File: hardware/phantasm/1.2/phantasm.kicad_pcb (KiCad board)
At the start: 4 copper layers, 58.3 x 32 mm, 33 parts, among them J1 TBC05-02-1-G-G +5V IN ~1A, J2 TBC05-03-1-G-G LED DI/SIG_GND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, J3A TBC05-03-1-G-G SYNC in, J3B TBC05-03-1-G-G SYNC out, J4 debug, U1 74AHCT125

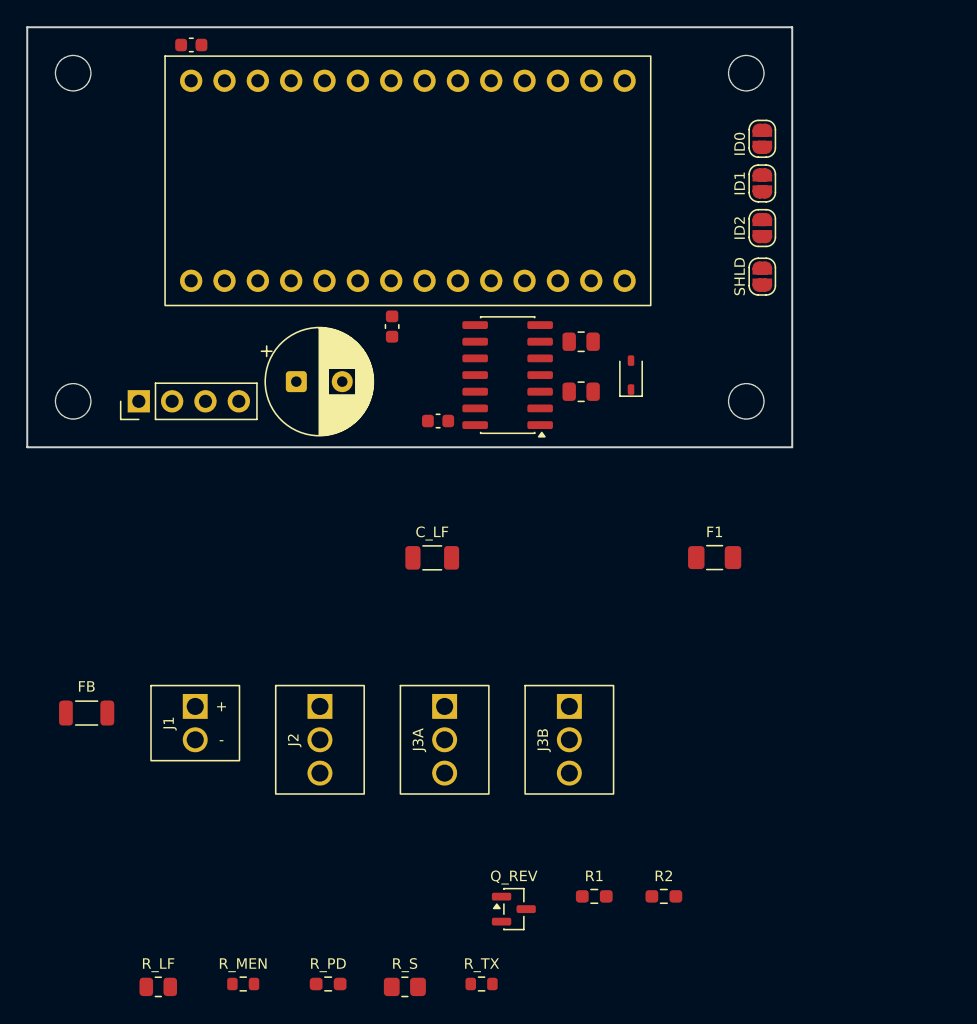
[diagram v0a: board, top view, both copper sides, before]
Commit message: pcb: enforce edge connector placement and wire clearance
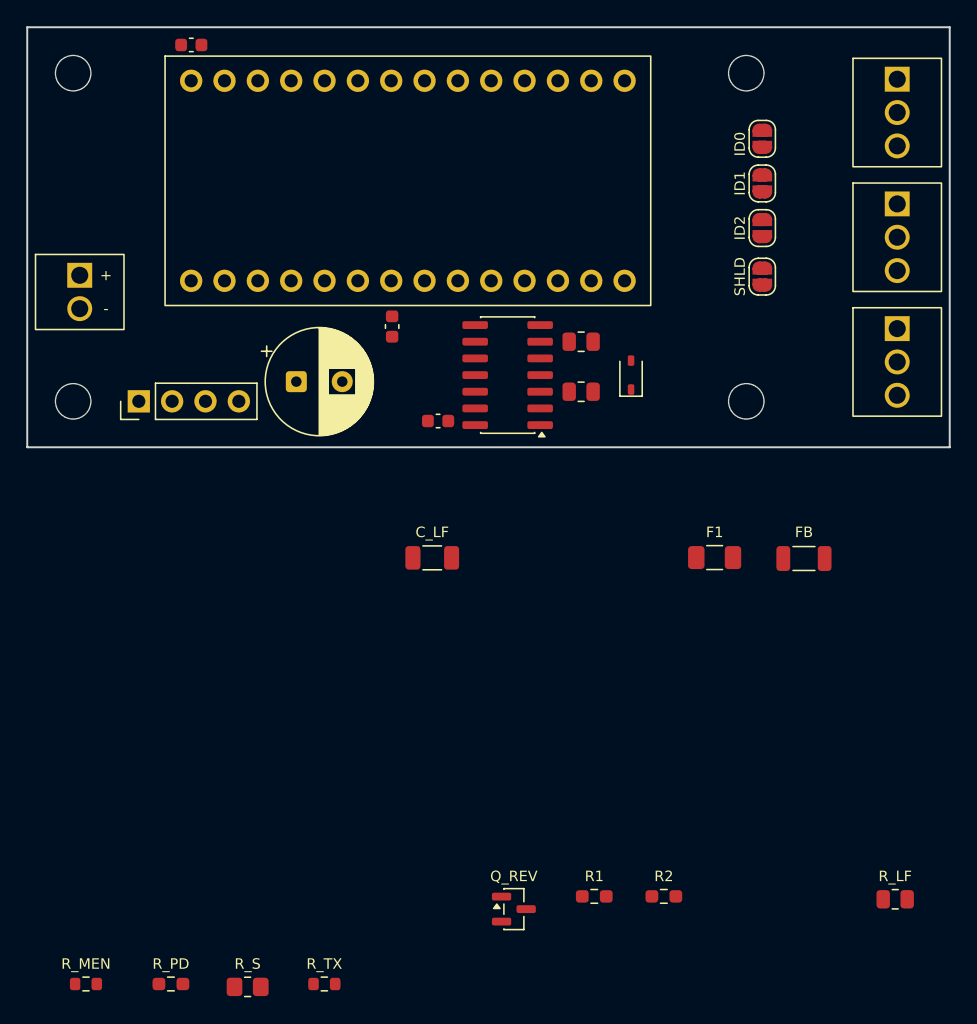
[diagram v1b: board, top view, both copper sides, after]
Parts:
- moved J2 64.9 mm to (66.3, 3.96)
- moved R_LF 56.5 mm to (66.1, 66.4)
- moved FB 55.9 mm to (59.2, 40.5)
- moved J3A 51.5 mm to (66.3, 13.5)
- moved J3B 38.1 mm to (66.3, 23.0)
- moved J1 34.0 mm to (4.00, 18.9)
- moved R_PD 12.0 mm to (10.9, 72.9)
- moved R_S 12.0 mm to (16.8, 73.1)
- moved R_TX 12.0 mm to (22.6, 72.9)
- moved R_MEN 12.0 mm to (4.47, 72.9)
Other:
- board size 58.3 x 32 mm -> 70.3 x 32 mm
- board text added: "LED OUT"
- board text added: "PHANTASM segment board UNPLACED - 70.28x32mm outline (width <=35mm); mechanical and signal-integrity placements locked"
- board text added: "PWR"
- board text added: "SYNC IN"
- board text added: "SYNC OUT"
- board text removed: "PHANTASM segment board UNPLACED - 58.28x32mm outline (width <=35mm); mechanical and signal-integrity placements locked"

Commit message: pcb: fit protected terminal bodies within the original outline
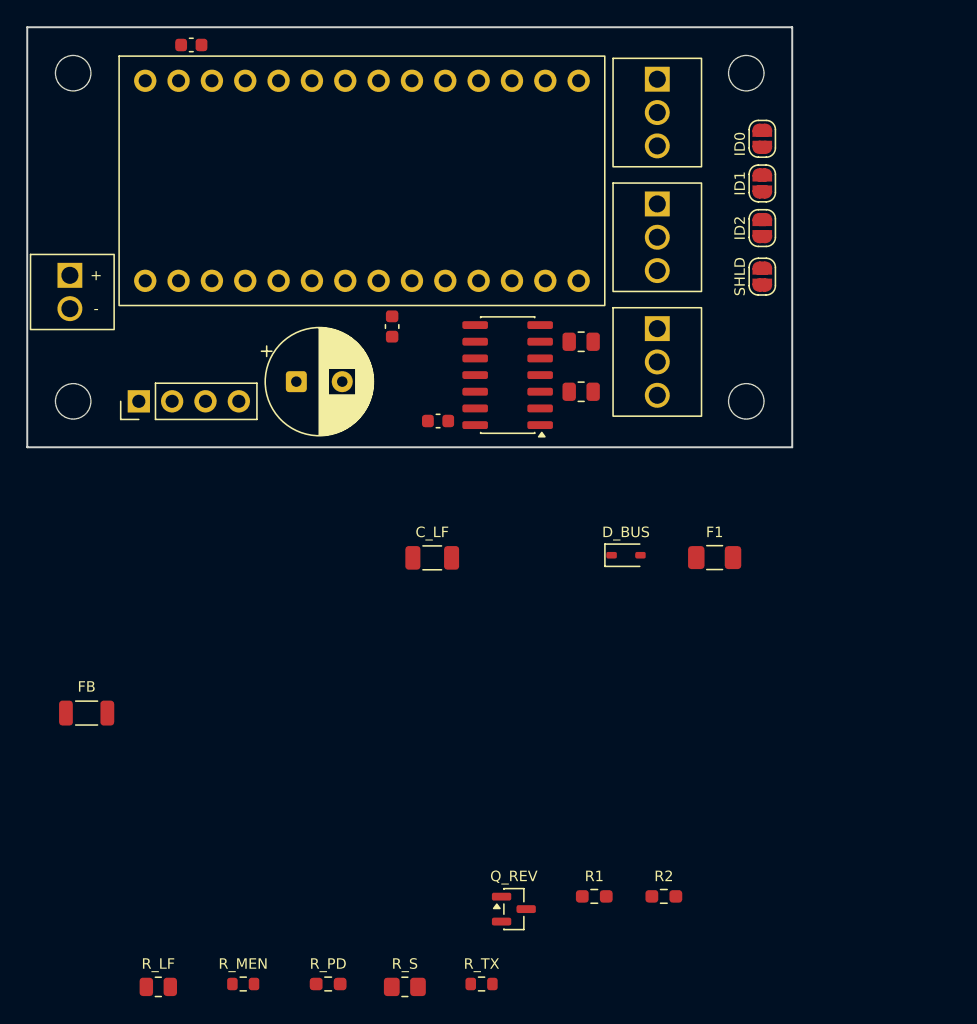
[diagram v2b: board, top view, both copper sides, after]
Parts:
- moved R_LF 56.5 mm to (9.98, 73.1)
- moved FB 55.9 mm to (4.53, 52.2)
- moved J2 18.3 mm to (48.0, 3.96)
- moved J3A 18.3 mm to (48.0, 13.5)
- moved J3B 18.3 mm to (48.0, 23.0)
- moved D_BUS 13.7 mm to (45.6, 40.2), turned to 0 degrees
- moved R_PD 12.0 mm to (22.9, 72.9)
- moved R_S 12.0 mm to (28.8, 73.1)
- moved R_TX 12.0 mm to (34.6, 72.9)
- moved R_MEN 12.0 mm to (16.5, 72.9)
- moved U_MCU 3.50 mm to (25.5, 11.7)
- moved J1 0.75 mm to (3.25, 18.9)
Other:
- board size 70.3 x 32 mm -> 58.3 x 32 mm
- board text added: "PHANTASM segment board UNPLACED - 58.28x32mm outline (width <=35mm); mechanical and signal-integrity placements locked"
- board text removed: "PHANTASM segment board UNPLACED - 70.28x32mm outline (width <=35mm); mechanical and signal-integrity placements locked"

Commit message: pcb: remove unused rev 1.2 debug header and serial connection
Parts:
- removed the H4 at (54.8, 28.5)
- H1: renamed from J4; value debug -> M2.5; footprint Connector_PinHeader_2.54mm:PinHeader_1x04_P2.54mm_Vertical -> MountingHole:MountingHole_2.7mm_M2.5
- moved H3 57.0 mm to (54.8, 3.50)
- moved H1 25.5 mm to (3.50, 3.50), turned to 0 degrees
- moved H2 25.0 mm to (3.50, 28.5)
- moved H4 25.0 mm to (54.8, 28.5)
- moved R1 3.42 mm to (43.2, 62.8)
- moved R2 3.42 mm to (48.5, 62.8)
- moved R_LF 3.42 mm to (9.98, 69.7)
- moved R_MEN 3.42 mm to (16.5, 69.5)
- moved R_PD 3.42 mm to (22.9, 69.5)
- moved R_S 3.42 mm to (28.8, 69.7)
- moved R_TX 3.42 mm to (34.6, 69.5)
- moved Q_REV 3.41 mm to (37.1, 63.8)
- renumbered H1 to H2, H2 to H3, H3 to H4
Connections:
- U_MCU pad 1: /SERIAL1_TX -> unconnected-(U_MCU-D1/TX1-Pad1)

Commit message: pcb: clarify bypass parents and enforce upload via minimum
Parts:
- C_DEC2: renamed from R_TX; value 10k -> 0.1uF; footprint Resistor_SMD:R_0603_1608Metric -> Capacitor_SMD:C_0603_1608Metric
- R_D1: renamed from U1; value 74AHCT125 -> 33R; footprint Package_SO:SOIC-14_3.9x8.7mm_P1.27mm -> Resistor_SMD:R_0805_2012Metric
- R_S: renamed from R_D2; value 33R -> 100R; footprint Resistor_SMD:R_0805_2012Metric -> Resistor_SMD:R_0805_2012Metric_Pad1.20x1.40mm_HandSolder
- R_TX: renamed from R_S; value 100R -> 10k; footprint Resistor_SMD:R_0805_2012Metric_Pad1.20x1.40mm_HandSolder -> Resistor_SMD:R_0603_1608Metric
- U1: renamed from U_MCU; value Teensy4.0 -> 74AHCT125; footprint phantasm:Teensy4.0 -> Package_SO:SOIC-14_3.9x8.7mm_P1.27mm
- U_MCU: renamed from C_DEC1; value 0.1uF -> Teensy4.0; footprint Capacitor_SMD:C_0603_1608Metric -> phantasm:Teensy4.0
- moved R_S 47.7 mm to (28.8, 69.7), turned to 0 degrees
- moved C_DEC2 39.6 mm to (31.3, 30.0), turned to 180 degrees
- moved C_DEC1 34.3 mm to (12.5, 1.35), turned to 0 degrees
- moved U1 18.5 mm to (36.6, 26.5), turned to 180 degrees
- moved U_MCU 16.6 mm to (25.5, 11.7)
- moved R_TX 5.85 mm to (34.6, 69.5)
- moved R_D1 5.74 mm to (42.2, 27.8)
- moved R_D2 3.81 mm to (42.2, 24.0)
- renumbered C_DEC2 to C_DEC1, R_D1 to R_D2
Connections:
- C_DEC2 pad 1: /SYNC_TX -> +5V_LOGIC
- R_D1 pad 1: GND -> /DATA
- R_D1 pad 2: /DATA_IN -> /DATA_SRC
- R_D2 pad 1: /DATA -> /CLK
- R_D2 pad 2: /DATA_SRC -> /CLK_SRC
- R_S pad 1: /CLK -> /SYNC_BUS
- R_S pad 2: /CLK_SRC -> /SYNC_SRC
- R_TX pad 1: /SYNC_BUS -> /SYNC_TX
- R_TX pad 2: /SYNC_SRC -> GND
- U1 pad 1: unconnected-(U_MCU-D1/TX1-Pad1) -> GND
- U1 pad 10: unconnected-(U_MCU-D10-Pad10) -> /MASTER_EN
- U1 pad 11: /DATA_IN -> /SYNC_PULLDOWN
- U1 pad 12: unconnected-(U_MCU-D12-Pad12) -> GND
- U1 pad 13: /CLK_IN -> /MASTER_EN
- U1 pad 14: unconnected-(U_MCU-D14-Pad14) -> +5V_LOGIC
- U1 pad 2: unconnected-(U_MCU-D2-Pad2) -> /DATA_IN
- U1 pad 3: /FRAME_SYNC -> /DATA_SRC
- U1 pad 4: /SYNC_TX -> GND
- U1 pad 5: /MASTER_EN -> /CLK_IN
- U1 pad 6: unconnected-(U_MCU-D6-Pad6) -> /CLK_SRC
- U1 pad 7: unconnected-(U_MCU-D7-Pad7) -> GND
- U1 pad 8: unconnected-(U_MCU-D8-Pad8) -> /SYNC_SRC
- U1 pad 9: unconnected-(U_MCU-D9-Pad9) -> /SYNC_TX
- U_MCU pad 1: +5V_LOGIC -> unconnected-(U_MCU-D1/TX1-Pad1)
- U_MCU pad 2: GND -> unconnected-(U_MCU-D2-Pad2)

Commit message: pcb: keep locked decouplers within 3 mm of supply pins
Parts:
- moved C_DEC1 2.75 mm to (9.75, 1.35)
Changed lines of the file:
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@@
 	(footprint "Capacitor_SMD:C_0603_1608Metric"
 		(locked yes)
-		(at 12.5 1.35 0)
+		(at 9.75 1.35 0)
 		(layer "F.Cu")
 		(descr "Capacitor SMD 0603 (1608 Metric), square (rectangular) end terminal, IPC-7351 nominal, (Body size source: IPC-SM-782 page 76, https://www.pcb-3d.com/wordpress/wp-content/uploads/ipc-sm-782a_amendment_1_and_2.pdf)")

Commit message: pcb: label every signal terminal pin (finding 81)
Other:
- board text added: "C"
- board text added: "D"
- board text added: "G"
- board text added: "H"
- board text added: "S"
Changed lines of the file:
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@@
 		(embedded_fonts no)
 	)
+	(gr_text "D" (at 52.5 3.96 0) (layer "F.SilkS") (effects (font (size 0.8 0.8) (thickness 0.15))))
+	(gr_text "G" (at 52.5 6.50 0) (layer "F.SilkS") (effects (font (size 0.8 0.8) (thickness 0.15))))
+	(gr_text "C" (at 52.5 9.04 0) (layer "F.SilkS") (effects (font (size 0.8 0.8) (thickness 0.15))))
+	(gr_text "S" (at 52.5 13.46 0) (layer "F.SilkS") (effects (font (size 0.8 0.8) (thickness 0.15))))
+	(gr_text "G" (at 52.5 16.00 0) (layer "F.SilkS") (effects (font (size 0.8 0.8) (thickness 0.15))))
+	(gr_text "H" (at 52.5 18.54 0) (layer "F.SilkS") (effects (font (size 0.8 0.8) (thickness 0.15))))
+	(gr_text "S" (at 52.5 22.96 0) (layer "F.SilkS") (effects (font (size 0.8 0.8) (thickness 0.15))))
+	(gr_text "G" (at 52.5 25.50 0) (layer "F.SilkS") (effects (font (size 0.8 0.8) (thickness 0.15))))
+	(gr_text "H" (at 52.5 28.04 0) (layer "F.SilkS") (effects (font (size 0.8 0.8) (thickness 0.15))))
 )

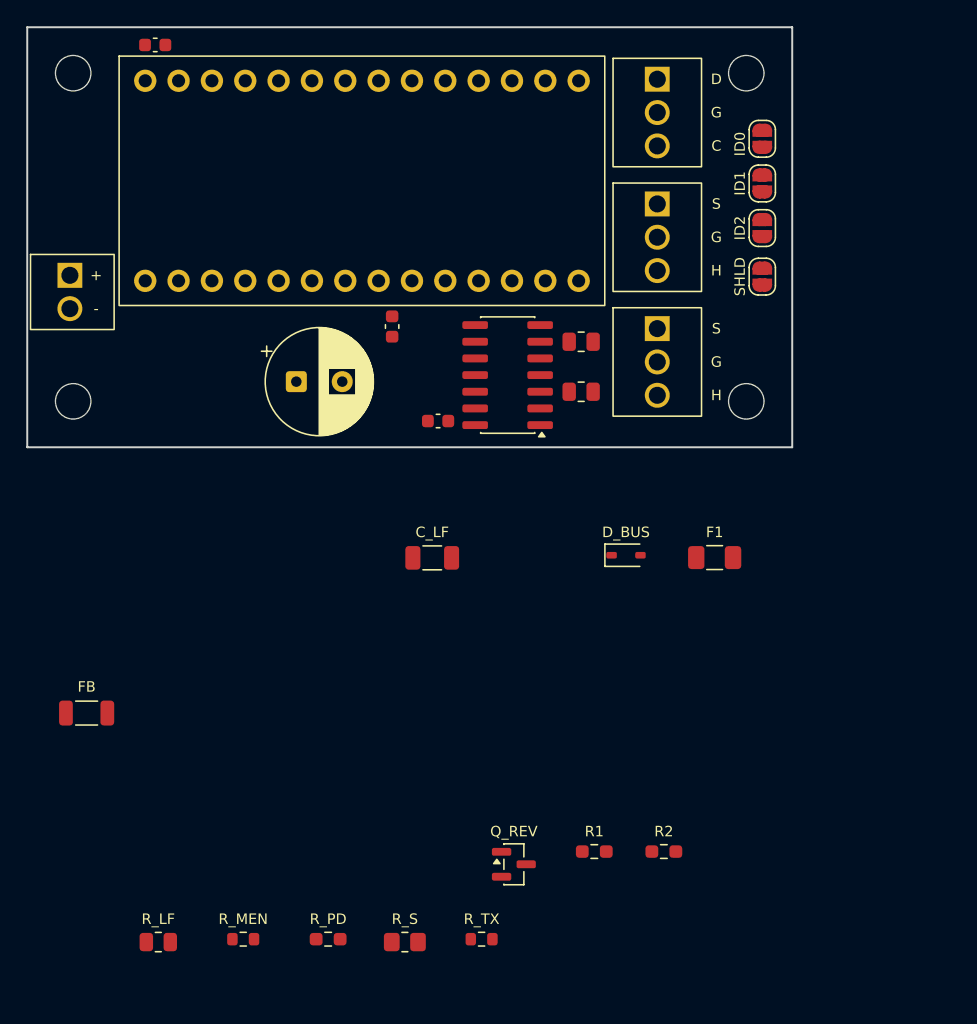
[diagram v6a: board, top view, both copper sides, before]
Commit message: pcb: pre-route the sync receive filter beside D3 (finding 4)
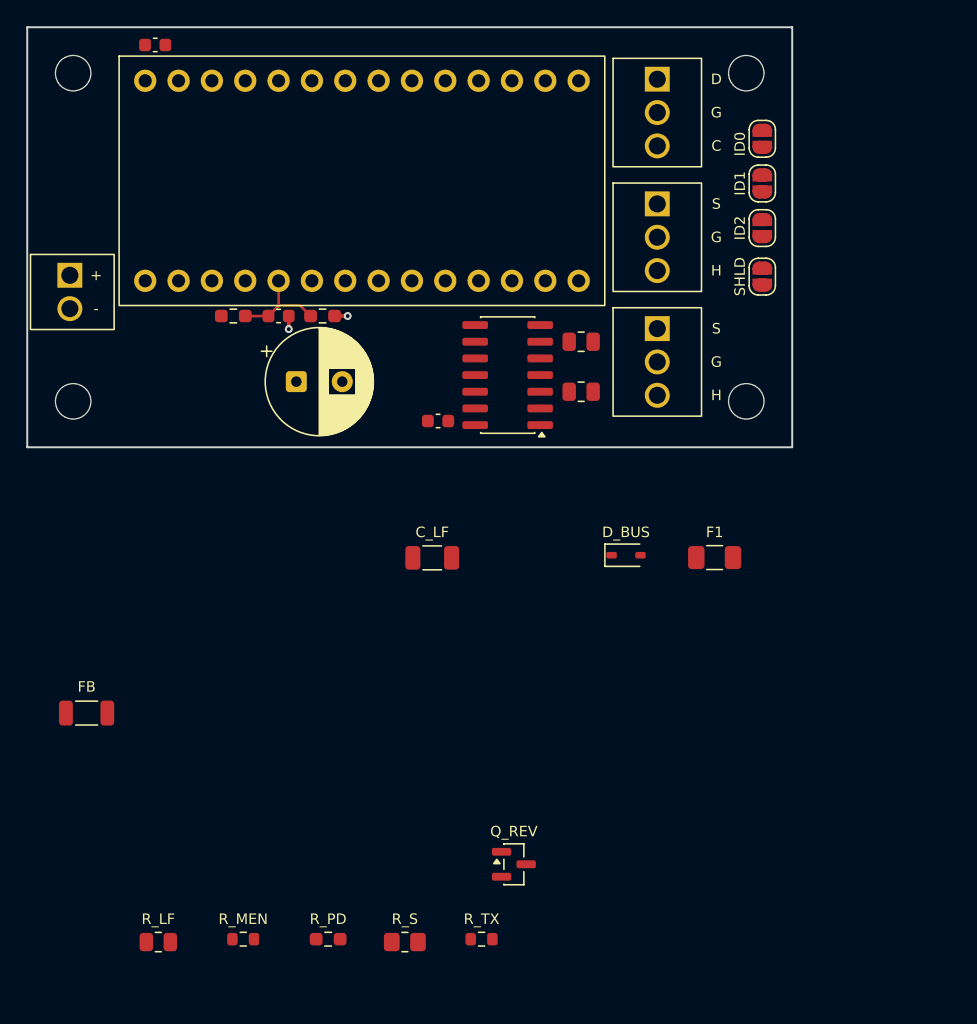
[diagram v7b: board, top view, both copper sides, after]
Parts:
- moved R1 49.2 mm to (15.7, 22.0)
- moved R2 48.4 mm to (22.5, 22.0)
- moved C_SYNC 8.69 mm to (19.1, 22.0), turned to 0 degrees
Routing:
- net /FRAME_SYNC: track 0.00 -> 8.64 mm
- net GND: track 0.00 -> 2.00 mm, vias 0 -> 2
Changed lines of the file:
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@@
 	(gr_text "ID2" (at 54.3 15.3 90) (layer "F.SilkS") (effects (font (size 0.8 0.8) (thickness 0.15))))
 	(gr_text "SHLD" (at 54.3 19 90) (layer "F.SilkS") (effects (font (size 0.8 0.8) (thickness 0.15))))
+	(gr_text "D" (at 52.5 3.96 0) (layer "F.SilkS") (effects (font (size 0.8 0.8) (thickness 0.15))))
+	(gr_text "G" (at 52.5 6.5 0) (layer "F.SilkS") (effects (font (size 0.8 0.8) (thickness 0.15))))
+	(gr_text "C" (at 52.5 9.04 0) (layer "F.SilkS") (effects (font (size 0.8 0.8) (thickness 0.15))))
+	(gr_text "S" (at 52.5 13.46 0) (layer "F.SilkS") (effects (font (size 0.8 0.8) (thickness 0.15))))
+	(gr_text "G" (at 52.5 16 0) (layer "F.SilkS") (effects (font (size 0.8 0.8) (thickness 0.15))))
+	(gr_text "H" (at 52.5 18.54 0) (layer "F.SilkS") (effects (font (size 0.8 0.8) (thickness 0.15))))
+	(gr_text "S" (at 52.5 22.96 0) (layer "F.SilkS") (effects (font (size 0.8 0.8) (thickness 0.15))))
+	(gr_text "G" (at 52.5 25.5 0) (layer "F.SilkS") (effects (font (size 0.8 0.8) (thickness 0.15))))
+	(gr_text "H" (at 52.5 28.04 0) (layer "F.SilkS") (effects (font (size 0.8 0.8) (thickness 0.15))))
 	(gr_text "PWR" (at 5.25 20.17 90) (layer "B.SilkS") (effects (font (size 0.8 0.8) (thickness 0.15)) (justify mirror)))
 	(gr_text "LED OUT" (at 46 6.5 90) (layer "B.SilkS") (effects (font (size 0.8 0.8) (thickness 0.15)) (justify mirror)))
@@
 	)
 	(footprint "Resistor_SMD:R_0603_1608Metric_Pad0.98x0.95mm_HandSolder"
+		(locked yes)
+		(at 15.7 22 0)
 		(layer "F.Cu")
-		(at 43.2 62.8 0)
 		(descr "Resistor SMD 0603 (1608 Metric), square (rectangular) end terminal, IPC-7351 nominal with elongated pad for handsoldering. (Body size source: IPC-SM-782 page 72, https://www.pcb-3d.com/wordpress/wp-content/uploads/ipc-sm-782a_amendment_1_and_2.pdf)")
 		(tags "resistor handsolder")
@@
 			(at 0 -1.53 0.0)
 			(layer "F.SilkS")
+			(hide yes)
 			(effects
 				(font
@@
 	)
 	(footprint "Resistor_SMD:R_0603_1608Metric_Pad0.98x0.95mm_HandSolder"
+		(locked yes)
+		(at 22.5 22 0)
 		(layer "F.Cu")
-		(at 48.5 62.8 0)
 		(descr "Resistor SMD 0603 (1608 Metric), square (rectangular) end terminal, IPC-7351 nominal with elongated pad for handsoldering. (Body size source: IPC-SM-782 page 72, https://www.pcb-3d.com/wordpress/wp-content/uploads/ipc-sm-782a_amendment_1_and_2.pdf)")
 		(tags "resistor handsolder")
@@
 			(at 0 -1.53 0.0)
 			(layer "F.SilkS")
+			(hide yes)
 			(effects
 				(font
@@
 	(footprint "Capacitor_SMD:C_0603_1608Metric"
 		(locked yes)
-		(at 27.8 22.8 90)
+		(at 19.15 22 0)
 		(layer "F.Cu")
 		(descr "Capacitor SMD 0603 (1608 Metric), square (rectangular) end terminal, IPC-7351 nominal, (Body size source: IPC-SM-782 page 76, https://www.pcb-3d.com/wordpress/wp-content/uploads/ipc-sm-782a_amendment_1_and_2.pdf)")
 		(tags "capacitor")
 		(property "Reference" "C_SYNC"
-			(at 0 -1.53 90.0)
+			(at 0 -1.53 0.0)
 			(layer "F.SilkS")
 			(hide yes)
@@
 		)
 		(pad "1" smd roundrect
-			(at -0.775 0 90)
+			(at -0.775 0)
 			(size 0.9 0.95)
 			(layers "F.Cu" "F.Mask" "F.Paste")
@@
 		)
 		(pad "2" smd roundrect
-			(at 0.775 0 90)
+			(at 0.775 0)
 			(size 0.9 0.95)
 			(layers "F.Cu" "F.Mask" "F.Paste")
@@
 		(embedded_fonts no)
 	)
-	(gr_text "D" (at 52.5 3.96 0) (layer "F.SilkS") (effects (font (size 0.8 0.8) (thickness 0.15))))
-	(gr_text "G" (at 52.5 6.50 0) (layer "F.SilkS") (effects (font (size 0.8 0.8) (thickness 0.15))))
-	(gr_text "C" (at 52.5 9.04 0) (layer "F.SilkS") (effects (font (size 0.8 0.8) (thickness 0.15))))
-	(gr_text "S" (at 52.5 13.46 0) (layer "F.SilkS") (effects (font (size 0.8 0.8) (thickness 0.15))))
-	(gr_text "G" (at 52.5 16.00 0) (layer "F.SilkS") (effects (font (size 0.8 0.8) (thickness 0.15))))
-	(gr_text "H" (at 52.5 18.54 0) (layer "F.SilkS") (effects (font (size 0.8 0.8) (thickness 0.15))))
-	(gr_text "S" (at 52.5 22.96 0) (layer "F.SilkS") (effects (font (size 0.8 0.8) (thickness 0.15))))
-	(gr_text "G" (at 52.5 25.50 0) (layer "F.SilkS") (effects (font (size 0.8 0.8) (thickness 0.15))))
-	(gr_text "H" (at 52.5 28.04 0) (layer "F.SilkS") (effects (font (size 0.8 0.8) (thickness 0.15))))
+	(segment (start 19.15 19.32) (end 19.15 21.225) (width 0.2) (layer "F.Cu") (net 12) (locked yes))
+	(segment (start 19.15 21.225) (end 18.375 22) (width 0.2) (layer "F.Cu") (net 12) (locked yes))
+	(segment (start 16.6125 22) (end 18.375 22) (width 0.2) (layer "F.Cu") (net 12) (locked yes))
+	(segment (start 21.5875 22) (end 20.7875 21.2) (width 0.2) (layer "F.Cu") (net 12) (locked yes))
+	(segment (start 20.7875 21.2) (end 19.175 21.2) (width 0.2) (layer "F.Cu") (net 12) (locked yes))
+	(segment (start 19.175 21.2) (end 18.375 22) (width 0.2) (layer "F.Cu") (net 12) (locked yes))
+	(segment (start 19.925 22) (end 19.925 23) (width 0.3) (layer "F.Cu") (net 23) (locked yes))
+	(via (at 19.925 23) (size 0.6) (drill 0.3) (layers "F.Cu" "B.Cu") (net 23) (locked yes))
+	(segment (start 23.4125 22) (end 24.4125 22) (width 0.3) (layer "F.Cu") (net 23) (locked yes))
+	(via (at 24.4125 22) (size 0.6) (drill 0.3) (layers "F.Cu" "B.Cu") (net 23) (locked yes))
 )
